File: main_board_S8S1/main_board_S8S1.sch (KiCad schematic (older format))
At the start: 47 parts

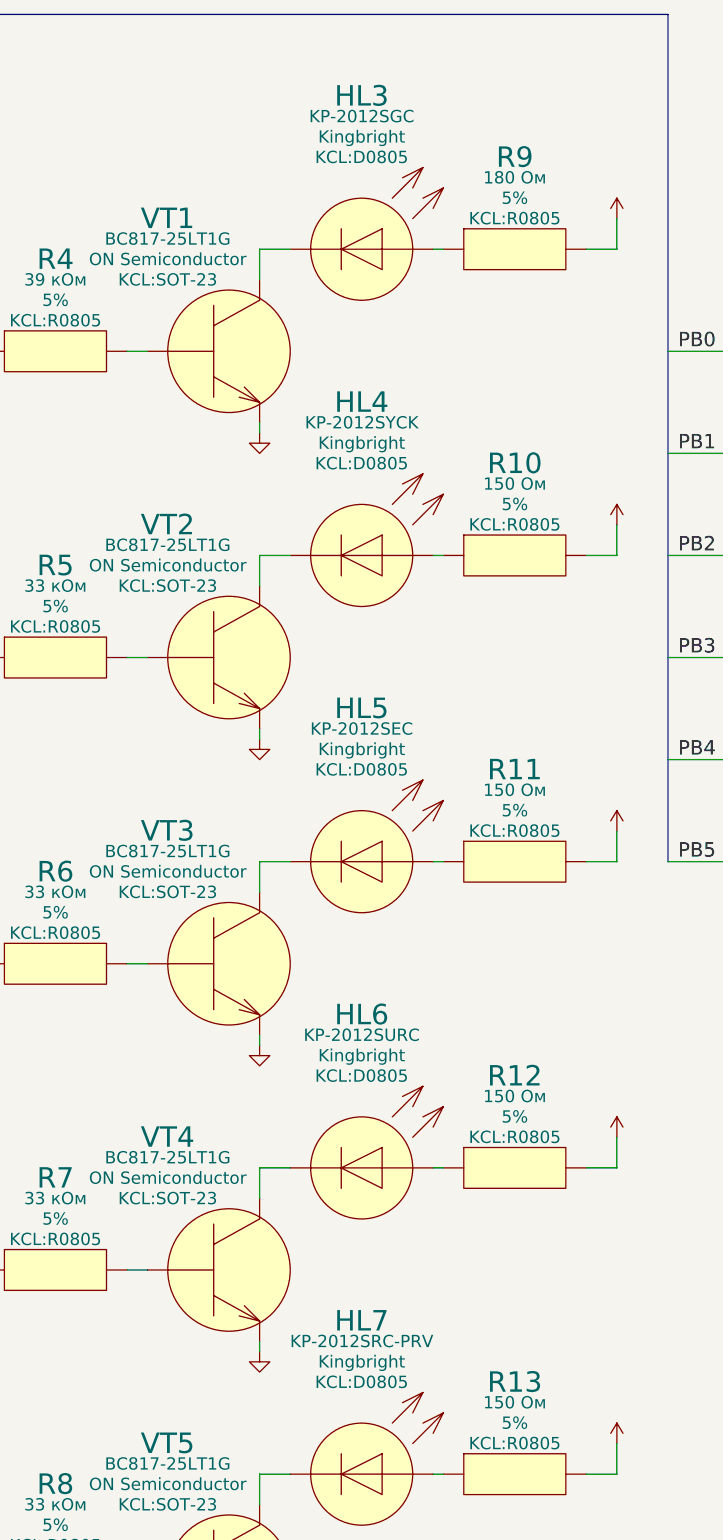
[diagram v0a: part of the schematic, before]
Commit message: Обновлены футпринты светодиодов
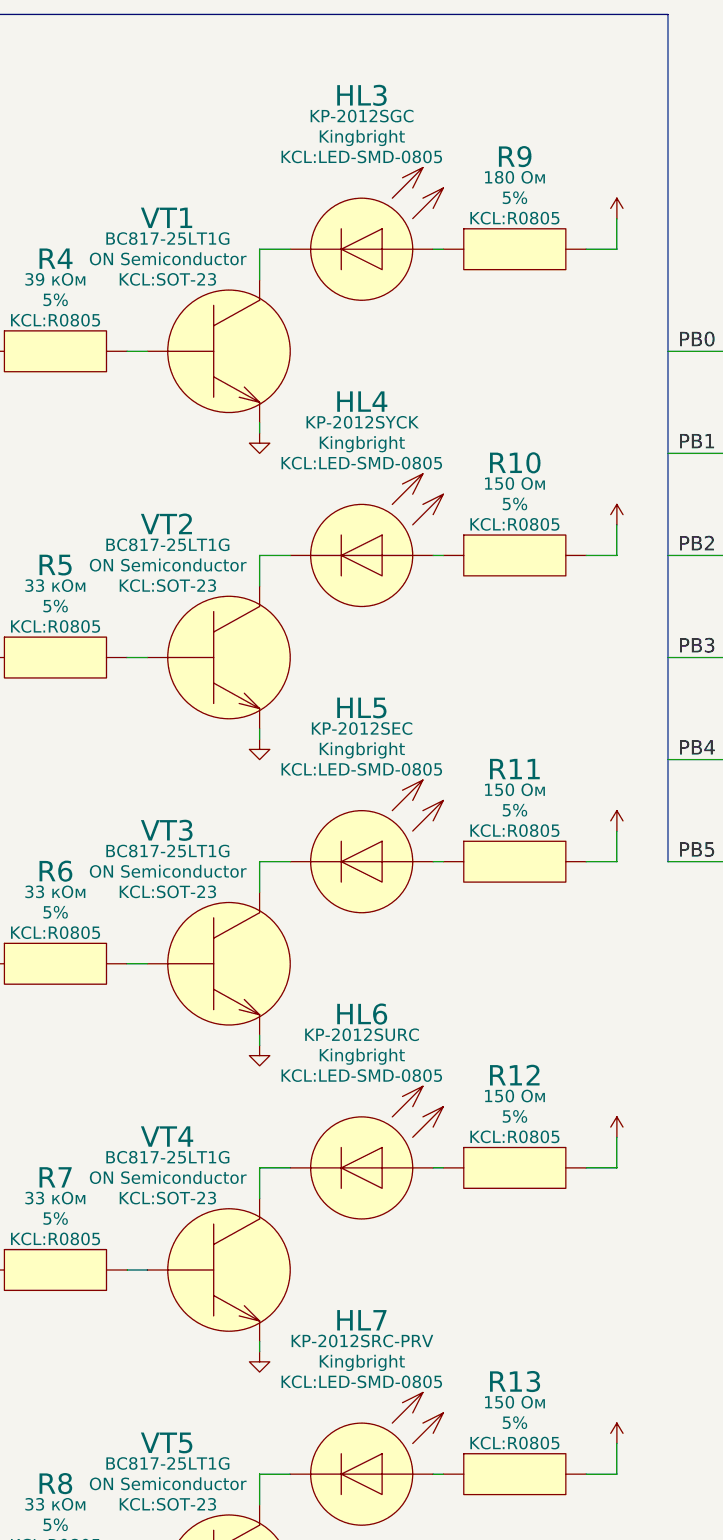
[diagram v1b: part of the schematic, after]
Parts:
- HL3, HL4, HL5, HL6, HL7: footprint KCL:D0805 -> KCL:LED-SMD-0805
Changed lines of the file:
@@
 Sheet 1 1
 Title "main_board_S8S1"
-Date "2018-08-13"
+Date "2018-08-18"
 Rev "2"
 Comp "Igor Vladimirovich Ivanov"
@@
 F 0 "HL3" H 11750 2650 100 0000 C CNN
 F 1 "DIODE_LIGHT-EMITTING_LEFT" H 11750 2550 100 0001 C CNN
-F 2 "KCL:D0805" H 11750 2350 60  0000 C CNN
+F 2 "KCL:LED-SMD-0805" H 11750 2350 60  0000 C CNN
 F 3 "" H 11550 2240 60  0001 C CNN
 F 4 "KP-2012SGC" H 11750 2550 60  0000 C CNN "Product"
@@
 F 0 "HL4" H 11750 4150 100 0000 C CNN
 F 1 "DIODE_LIGHT-EMITTING_LEFT" H 11750 4050 100 0001 C CNN
-F 2 "KCL:D0805" H 11750 3850 60  0000 C CNN
+F 2 "KCL:LED-SMD-0805" H 11750 3850 60  0000 C CNN
 F 3 "" H 11550 3740 60  0001 C CNN
 F 4 "KP-2012SYCK" H 11750 4050 60  0000 C CNN "Product"
@@
 F 0 "HL5" H 11750 5650 100 0000 C CNN
 F 1 "DIODE_LIGHT-EMITTING_LEFT" H 11750 5550 100 0001 C CNN
-F 2 "KCL:D0805" H 11750 5350 60  0000 C CNN
+F 2 "KCL:LED-SMD-0805" H 11750 5350 60  0000 C CNN
 F 3 "" H 11550 5240 60  0001 C CNN
 F 4 "KP-2012SEC" H 11750 5550 60  0000 C CNN "Product"
@@
 F 0 "HL6" H 11750 7150 100 0000 C CNN
 F 1 "DIODE_LIGHT-EMITTING_LEFT" H 11750 7050 100 0001 C CNN
-F 2 "KCL:D0805" H 11750 6850 60  0000 C CNN
+F 2 "KCL:LED-SMD-0805" H 11750 6850 60  0000 C CNN
 F 3 "" H 11550 6740 60  0001 C CNN
 F 4 "KP-2012SURC" H 11750 7050 60  0000 C CNN "Product"
@@
 F 0 "HL7" H 11750 8650 100 0000 C CNN
 F 1 "DIODE_LIGHT-EMITTING_LEFT" H 11750 8550 100 0001 C CNN
-F 2 "KCL:D0805" H 11750 8350 60  0000 C CNN
+F 2 "KCL:LED-SMD-0805" H 11750 8350 60  0000 C CNN
 F 3 "" H 11550 8240 60  0001 C CNN
 F 4 "KP-2012SRC-PRV" H 11750 8550 60  0000 C CNN "Product"

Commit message: Обновлены футпринты светодиодов HL1, HL2
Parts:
- HL1, HL2: footprint KCL:D0805 -> KCL:LED-SMD-0805
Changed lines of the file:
@@
 Sheet 1 1
 Title "main_board_S8S1"
-Date "2018-08-18"
+Date "2018-10-30"
 Rev "2"
 Comp "Igor Vladimirovich Ivanov"
@@
 F 0 "HL2" V 6600 10400 100 0000 L CNN
 F 1 "DIODE_LIGHT-EMITTING_LEFT" H 6750 10650 100 0001 C CNN
-F 2 "KCL:D0805" V 6900 10400 60  0000 L CNN
+F 2 "KCL:LED-SMD-0805" V 6900 10400 60  0000 L CNN
 F 3 "" H 6550 10340 60  0001 C CNN
 F 4 "FYLS-0805UWC" V 6700 10400 60  0000 L CNN "Product"
@@
 F 0 "HL1" V 5350 7850 100 0000 L CNN
 F 1 "DIODE_LIGHT-EMITTING_LEFT" H 5500 8100 100 0001 C CNN
-F 2 "KCL:D0805" V 5650 7850 60  0000 L CNN
+F 2 "KCL:LED-SMD-0805" V 5650 7850 60  0000 L CNN
 F 3 "" H 5300 7790 60  0001 C CNN
 F 4 "FYLS-0805BUBC" V 5450 7850 60  0000 L CNN "Product"

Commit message: Файл библиотеки символов переименован в соответствии с названием проекта
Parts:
- XP1, XP4: symbol KCPL:CONNECTOR_M_014_20_ДАННЫЕ -> main_board_S8S1:CONNECTOR_M_014_20_ДАННЫЕ
- XP2: symbol KCPL:CONNECTOR_M_BARREL_20_ПИТАНИЕ -> main_board_S8S1:CONNECTOR_M_BARREL_20_ПИТАНИЕ
- XP3: symbol KCPL:CONNECTOR_M_010_20_ПРОГРАММАТОР -> main_board_S8S1:CONNECTOR_M_010_20_ПРОГРАММАТОР
- XS1: symbol KCPL:CONNECTOR_F_002_20_КВАРЦ -> main_board_S8S1:CONNECTOR_F_002_20_КВАРЦ
- XS2: symbol KCPL:CONNECTOR_F_002_20_ПИТАНИЕ -> main_board_S8S1:CONNECTOR_F_002_20_ПИТАНИЕ
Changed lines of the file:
@@
 	4600 6450 4650 6450
 $Comp
-L KCPL:CONNECTOR_M_014_20_ДАННЫЕ XP4
+L main_board_S8S1:CONNECTOR_M_014_20_ДАННЫЕ XP4
 U 1 1 5AD7D10B
 P 14000 1900
@@
 $EndComp
 $Comp
-L KCPL:CONNECTOR_M_010_20_ПРОГРАММАТОР XP3
+L main_board_S8S1:CONNECTOR_M_010_20_ПРОГРАММАТОР XP3
 U 1 1 5AD7D48C
 P 5500 1900
@@
 $EndComp
 $Comp
-L KCPL:CONNECTOR_F_002_20_КВАРЦ XS1
+L main_board_S8S1:CONNECTOR_F_002_20_КВАРЦ XS1
 U 1 1 5AD7D71D
 P 3000 6400
@@
 $EndComp
 $Comp
-L KCPL:CONNECTOR_F_002_20_ПИТАНИЕ XS2
+L main_board_S8S1:CONNECTOR_F_002_20_ПИТАНИЕ XS2
 U 1 1 5AD7D7C6
 P 3000 10500
@@
 $EndComp
 $Comp
-L KCPL:CONNECTOR_M_BARREL_20_ПИТАНИЕ XP2
+L main_board_S8S1:CONNECTOR_M_BARREL_20_ПИТАНИЕ XP2
 U 1 1 5AD7D885
 P 3000 8750
@@
 $EndComp
 $Comp
-L KCPL:CONNECTOR_M_014_20_ДАННЫЕ XP1
+L main_board_S8S1:CONNECTOR_M_014_20_ДАННЫЕ XP1
 U 1 1 5AD7E6B0
 P 3000 1900

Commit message: В связи с доработкой библиотеки обновлено большинство футпринтов
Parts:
- C1, C2, C4, C5: footprint KCL:C0805 -> KCL:C-SMD-0805
- C3: footprint KCL:T3528 -> KCL:CP-SMD-3528
- DD1: footprint KCL:SO-08 -> KCL:P-SO-08
- L1: footprint KCL:SDR0805 -> KCL:L-SDR0805
- R1, R10, R11, R12, R13, R2, R3, R4, R5, R6, R7, R8, R9: footprint KCL:R0805 -> KCL:R-SMD-0805
- SA1, SA2: footprint KCL:SK-42D01-G -> KCL:SW-SK-42D01-G
- SA3: footprint KCL:NDI(R)-05 -> KCL:SW-NDI(R)-05
- SA3: footprint (none) -> KCL:SW-NDI(R)-05
- SB1: footprint KCL:07125 -> KCL:SW-07125
- VD1: footprint KCL:SOD-323 -> KCL:P-SOD-323
- VT1, VT2, VT3, VT4, VT5: footprint KCL:SOT-23 -> KCL:P-SOT-23
- XP1, XP4: footprint KCL:IDC-14MR -> KCL:CON-IDC-14MR
- XP2: footprint KCL:PJ-002B -> KCL:CON-PJ-002B
- XP3: footprint KCL:IDC-10MR -> KCL:CON-IDC-10MR
- XS1, XS2: footprint KCL:DG301R-5.0-02P -> KCL:CON-DG301R-5.0-02P
- XS3, XS4, XS5, XS6: footprint KCL:DA5 -> KCL:STA-DA5
